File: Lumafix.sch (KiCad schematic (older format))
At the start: 6 parts, among them U1 74LS14, U2 VICII, U3 VICII_Socket

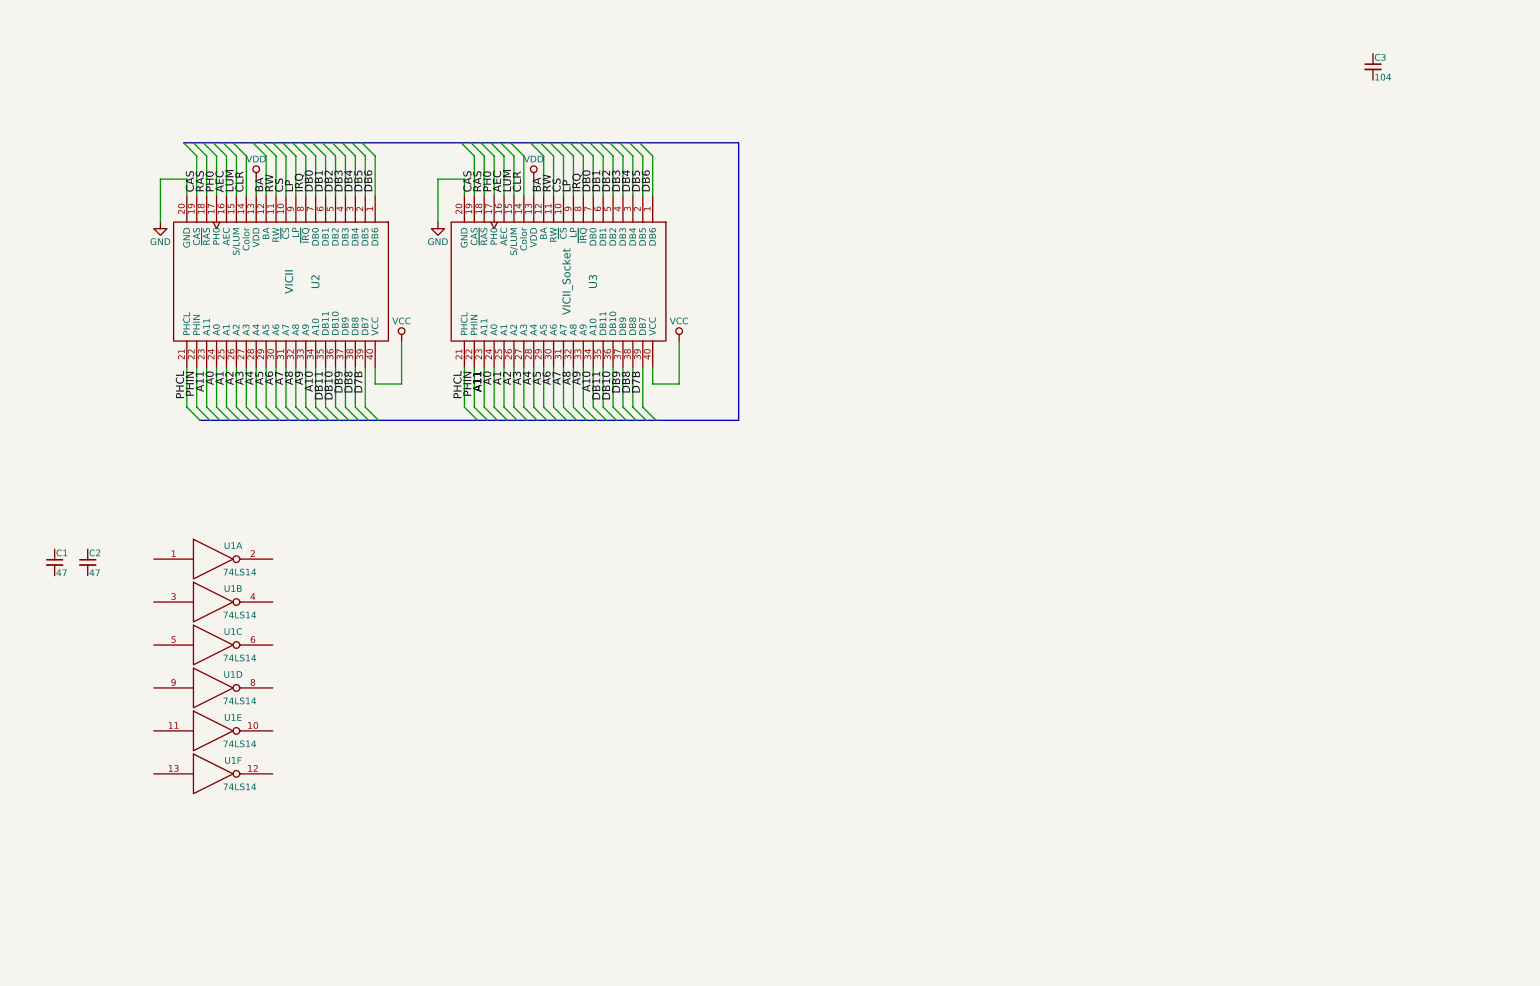
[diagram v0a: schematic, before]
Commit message: Schematic completed
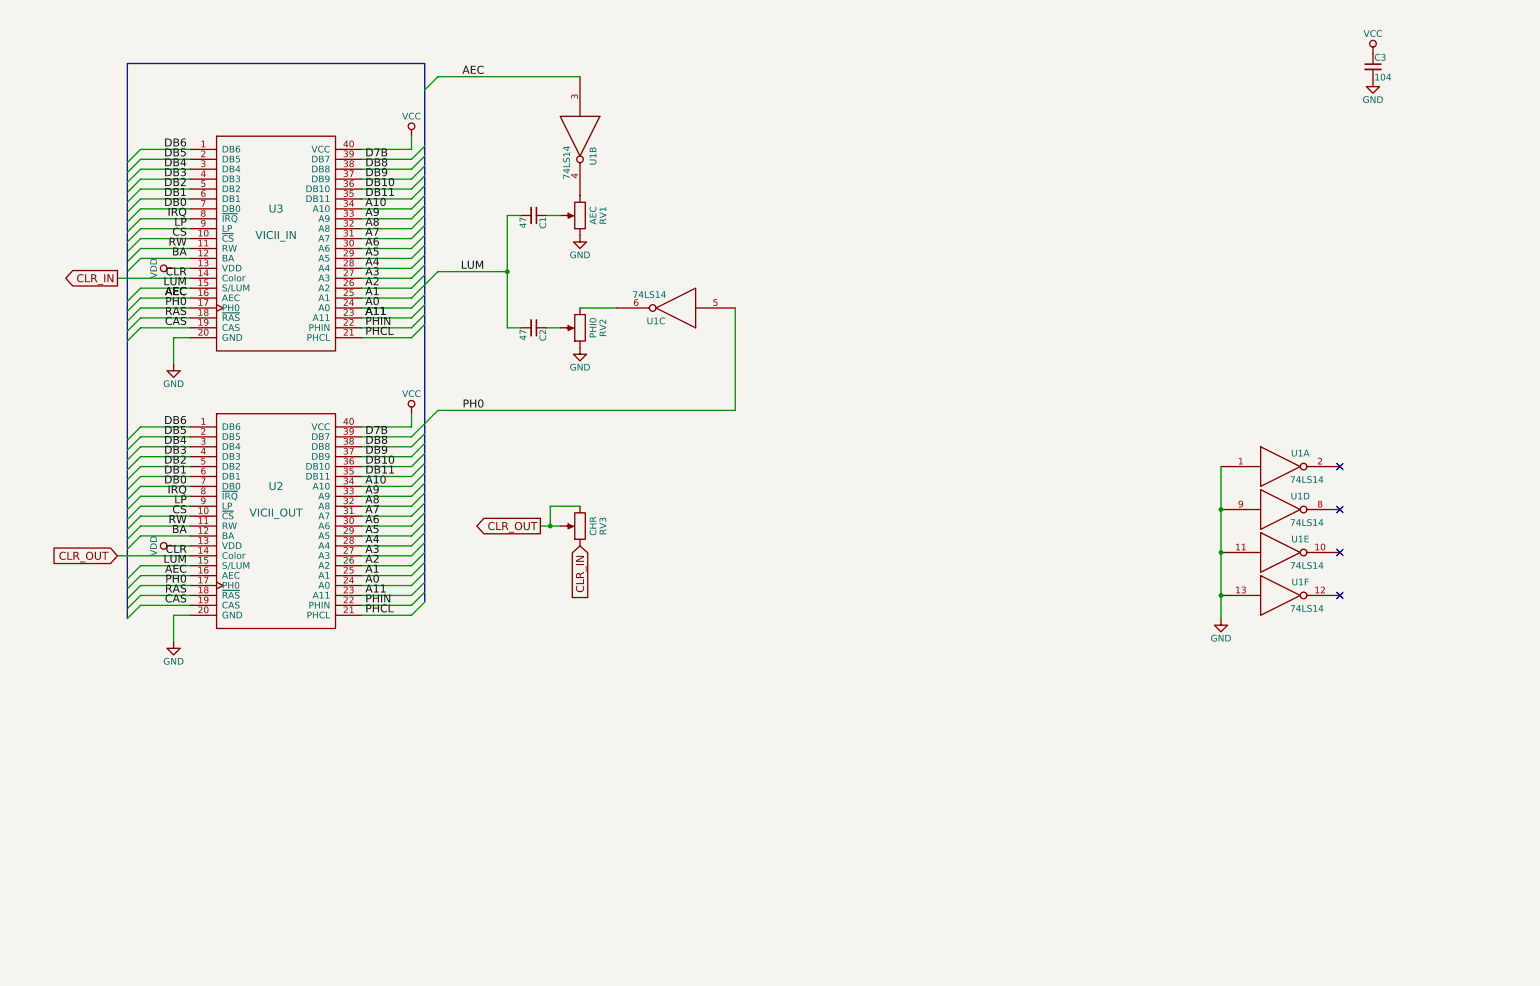
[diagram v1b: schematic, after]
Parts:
- added RV1: AEC, symbol POT
- added RV2: PHI0, symbol POT
- added RV3: CHR, symbol POT
- U2: value VICII -> VICII_OUT
- U3: value VICII_Socket -> VICII_IN
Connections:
- net AEC: now also U1.3
- net GND: now also C3.2, U1.1, U1.11, U1.13, U1.9, RV1.1, RV2.1
- net LUM: now also C1.2, C2.2
- net PH0: now also U1.5
- net VCC: now also C3.1
- net at U1.4: now also RV1.3
- net at U1.6: now also RV2.3
- net at C1.1: now also RV1.2
- net at C2.1: now also RV2.2
- net CLR renamed CLR_IN
- net CLR_IN: now also RV3.1, RV3.2, RV3.3
- no-connect marks 0 -> 4
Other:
- moved on the sheet: C1, C2, U1A, U1B, U1C, U1D, U1E, U1F, U2, U3

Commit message: PCB layout and gerber export
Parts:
- C1, C2, C3: footprint (none) -> Capacitors_THT:C_Disc_D4.7mm_W2.5mm_P5.00mm
- RV1, RV2, RV3: footprint (none) -> Potentiometers:Potentiometer_Trimmer_Bourns_3296W
- U1: footprint (none) -> Housings_DIP:DIP-14_W7.62mm_Socket
- U2: footprint (none) -> Housings_DIP:DIP-40_W15.24mm
- U3: footprint (none) -> Housings_DIP:DIP-40_W15.24mm_Socket
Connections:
- net CLR_IN: no longer RV3.2, RV3.3, U2.14 (Color)
- new net CLR_OUT: RV3.2, RV3.3, U2.14 (Color)
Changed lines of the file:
@@
 F 0 "U2" H 2525 4500 60  0000 C CNN
 F 1 "VICII_OUT" H 2525 4300 60  0000 C CNN
-F 2 "" H 2525 4300 60  0001 C CNN
+F 2 "Housings_DIP:DIP-40_W15.24mm" H 2525 4300 60  0001 C CNN
 F 3 "" H 2525 4300 60  0001 C CNN
 	1    2525 4300
@@
 F 0 "U1" H 10275 4050 50  0000 C CNN
 F 1 "74LS14" H 10325 3850 50  0000 C CNN
-F 2 "" H 10125 3950 50  0001 C CNN
+F 2 "Housings_DIP:DIP-14_W7.62mm_Socket" H 10125 3950 50  0001 C CNN
 F 3 "" H 10125 3950 50  0001 C CNN
 	1    10125 3950
@@
 F 0 "U1" H 4975 1550 50  0000 C CNN
 F 1 "74LS14" H 5025 1350 50  0000 C CNN
-F 2 "" H 4825 1450 50  0001 C CNN
+F 2 "Housings_DIP:DIP-14_W7.62mm_Socket" H 4825 1450 50  0001 C CNN
 F 3 "" H 4825 1450 50  0001 C CNN
 	2    4825 1450
@@
 F 0 "U1" H 5700 2850 50  0000 C CNN
 F 1 "74LS14" H 5750 2650 50  0000 C CNN
-F 2 "" H 5550 2750 50  0001 C CNN
+F 2 "Housings_DIP:DIP-14_W7.62mm_Socket" H 5550 2750 50  0001 C CNN
 F 3 "" H 5550 2750 50  0001 C CNN
 	3    5550 2750
@@
 F 0 "U1" H 10275 4375 50  0000 C CNN
 F 1 "74LS14" H 10325 4175 50  0000 C CNN
-F 2 "" H 10125 4275 50  0001 C CNN
+F 2 "Housings_DIP:DIP-14_W7.62mm_Socket" H 10125 4275 50  0001 C CNN
 F 3 "" H 10125 4275 50  0001 C CNN
 	4    10125 4275
@@
 F 0 "U1" H 10275 4700 50  0000 C CNN
 F 1 "74LS14" H 10325 4500 50  0000 C CNN
-F 2 "" H 10125 4600 50  0001 C CNN
+F 2 "Housings_DIP:DIP-14_W7.62mm_Socket" H 10125 4600 50  0001 C CNN
 F 3 "" H 10125 4600 50  0001 C CNN
 	5    10125 4600
@@
 F 0 "U1" H 10275 5025 50  0000 C CNN
 F 1 "74LS14" H 10325 4825 50  0000 C CNN
-F 2 "" H 10125 4925 50  0001 C CNN
+F 2 "Housings_DIP:DIP-14_W7.62mm_Socket" H 10125 4925 50  0001 C CNN
 F 3 "" H 10125 4925 50  0001 C CNN
 	6    10125 4925
@@
 F 0 "C1" H 4485 2120 50  0000 L CNN
 F 1 "47" H 4485 1970 50  0000 L CNN
-F 2 "" H 4475 2050 50  0001 C CNN
+F 2 "Capacitors_THT:C_Disc_D4.7mm_W2.5mm_P5.00mm" H 4475 2050 50  0001 C CNN
 F 3 "" H 4475 2050 50  0001 C CNN
 	1    4475 2050
@@
 F 0 "C2" H 4485 2970 50  0000 L CNN
 F 1 "47" H 4485 2820 50  0000 L CNN
-F 2 "" H 4475 2900 50  0001 C CNN
+F 2 "Capacitors_THT:C_Disc_D4.7mm_W2.5mm_P5.00mm" H 4475 2900 50  0001 C CNN
 F 3 "" H 4475 2900 50  0001 C CNN
 	1    4475 2900
@@
 F 0 "C3" H 10835 995 50  0000 L CNN
 F 1 "104" H 10835 845 50  0000 L CNN
-F 2 "" H 10825 925 50  0001 C CNN
+F 2 "Capacitors_THT:C_Disc_D4.7mm_W2.5mm_P5.00mm" H 10825 925 50  0001 C CNN
 F 3 "" H 10825 925 50  0001 C CNN
 	1    10825 925
@@
 Text Label 1850 4700 2    60   ~ 0
 LUM
-Text Label 1850 4625 2    60   ~ 0
-CLR
 Text Label 1850 4475 2    60   ~ 0
 BA
@@
 F 0 "U3" H 2525 2400 60  0000 C CNN
 F 1 "VICII_IN" H 2525 2200 60  0000 C CNN
-F 2 "" H 2525 2200 60  0001 C CNN
+F 2 "Housings_DIP:DIP-40_W15.24mm_Socket" H 2525 2200 60  0001 C CNN
 F 3 "" H 2525 2200 60  0001 C CNN
 	1    2525 2200
@@
 Text Label 1850 2600 2    60   ~ 0
 LUM
-Text Label 1850 2525 2    60   ~ 0
-CLR
 Text Label 1850 2375 2    60   ~ 0
 BA
@@
 F 0 "RV1" V 4650 2050 50  0000 C CNN
 F 1 "AEC" V 4725 2050 50  0000 C CNN
-F 2 "" H 4825 2050 50  0001 C CNN
+F 2 "Potentiometers:Potentiometer_Trimmer_Bourns_3296W" H 4825 2050 50  0001 C CNN
 F 3 "" H 4825 2050 50  0001 C CNN
 	1    4825 2050
@@
 F 0 "RV2" V 4650 2900 50  0000 C CNN
 F 1 "PHI0" V 4725 2900 50  0000 C CNN
-F 2 "" H 4825 2900 50  0001 C CNN
+F 2 "Potentiometers:Potentiometer_Trimmer_Bourns_3296W" H 4825 2900 50  0001 C CNN
 F 3 "" H 4825 2900 50  0001 C CNN
 	1    4825 2900
@@
 F 0 "RV3" V 4650 4400 50  0000 C CNN
 F 1 "CHR" V 4725 4400 50  0000 C CNN
-F 2 "" H 4825 4400 50  0001 C CNN
+F 2 "Potentiometers:Potentiometer_Trimmer_Bourns_3296W" H 4825 4400 50  0001 C CNN
 F 3 "" H 4825 4400 50  0001 C CNN
 	1    4825 4400
@@
 	3550 1550 3550 1450
 $Comp
-L GND #PWR?
+L GND #PWR07
 U 1 1 5B99D4D6
 P 4825 2200
-F 0 "#PWR?" H 4825 1950 50  0001 C CNN
+F 0 "#PWR07" H 4825 1950 50  0001 C CNN
 F 1 "GND" H 4825 2050 50  0000 C CNN
 F 2 "" H 4825 2200 50  0001 C CNN
@@
 $EndComp
 $Comp
-L GND #PWR?
+L GND #PWR08
 U 1 1 5B99D50B
 P 4825 3050
-F 0 "#PWR?" H 4825 2800 50  0001 C CNN
+F 0 "#PWR08" H 4825 2800 50  0001 C CNN
 F 1 "GND" H 4825 2900 50  0000 C CNN
 F 2 "" H 4825 3050 50  0001 C CNN
@@
 	6000 3525 6000 2750
 $Comp
-L GND #PWR?
+L GND #PWR09
 U 1 1 5B9A3666
 P 9675 5100
-F 0 "#PWR?" H 9675 4850 50  0001 C CNN
+F 0 "#PWR09" H 9675 4850 50  0001 C CNN
 F 1 "GND" H 9675 4950 50  0000 C CNN
 F 2 "" H 9675 5100 50  0001 C CNN
@@
 NoConn ~ 10575 4925
 $Comp
-L GND #PWR?
+L GND #PWR010
 U 1 1 5B9A40AD
 P 10825 1025
-F 0 "#PWR?" H 10825 775 50  0001 C CNN
+F 0 "#PWR010" H 10825 775 50  0001 C CNN
 F 1 "GND" H 10825 875 50  0000 C CNN
 F 2 "" H 10825 1025 50  0001 C CNN
@@
 $EndComp
 $Comp
-L VCC #PWR?
+L VCC #PWR011
 U 1 1 5B9A42CC
 P 10825 825
-F 0 "#PWR?" H 10825 675 50  0001 C CNN
+F 0 "#PWR011" H 10825 675 50  0001 C CNN
 F 1 "VCC" H 10825 975 50  0000 C CNN
 F 2 "" H 10825 825 50  0001 C CNN

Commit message: Exported schematic
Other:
- note added: "C64 Lumafix"
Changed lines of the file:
@@
 	1    0    0    -1
 $EndComp
+Text Notes 7375 7500 0    60   ~ 0
+C64 Lumafix
 $EndSCHEMATC

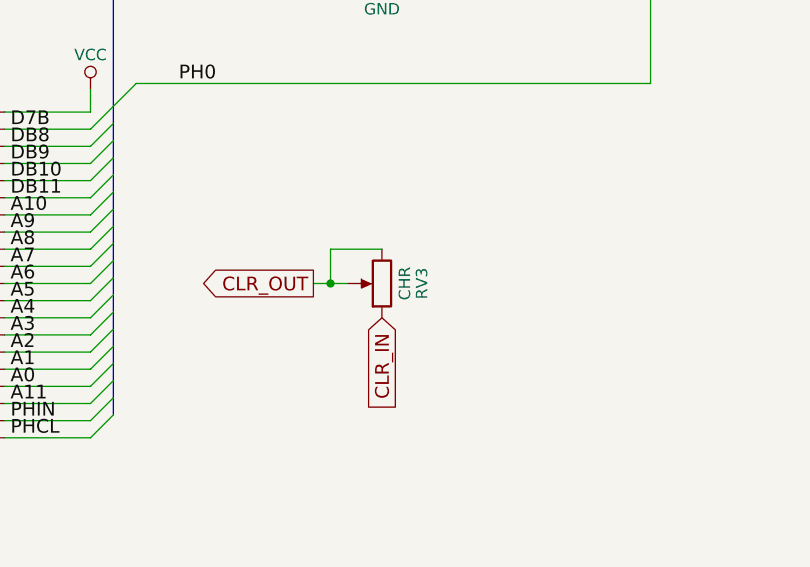
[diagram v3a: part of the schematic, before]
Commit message: Misspelled CLR on PCB, oops!
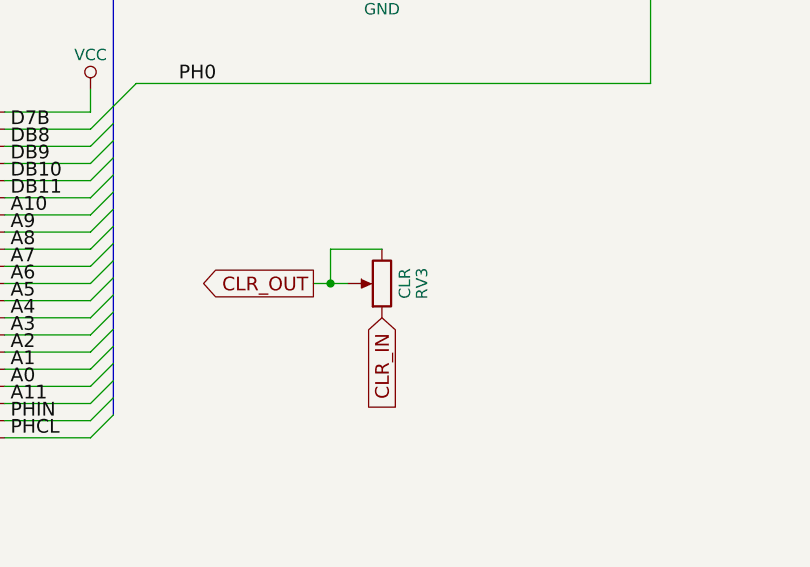
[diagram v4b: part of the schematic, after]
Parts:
- RV3: value CHR -> CLR
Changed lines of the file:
@@
 P 4825 4400
 F 0 "RV3" V 4650 4400 50  0000 C CNN
-F 1 "CHR" V 4725 4400 50  0000 C CNN
+F 1 "CLR" V 4725 4400 50  0000 C CNN
 F 2 "Potentiometers:Potentiometer_Trimmer_Bourns_3296W" H 4825 4400 50  0001 C CNN
 F 3 "" H 4825 4400 50  0001 C CNN

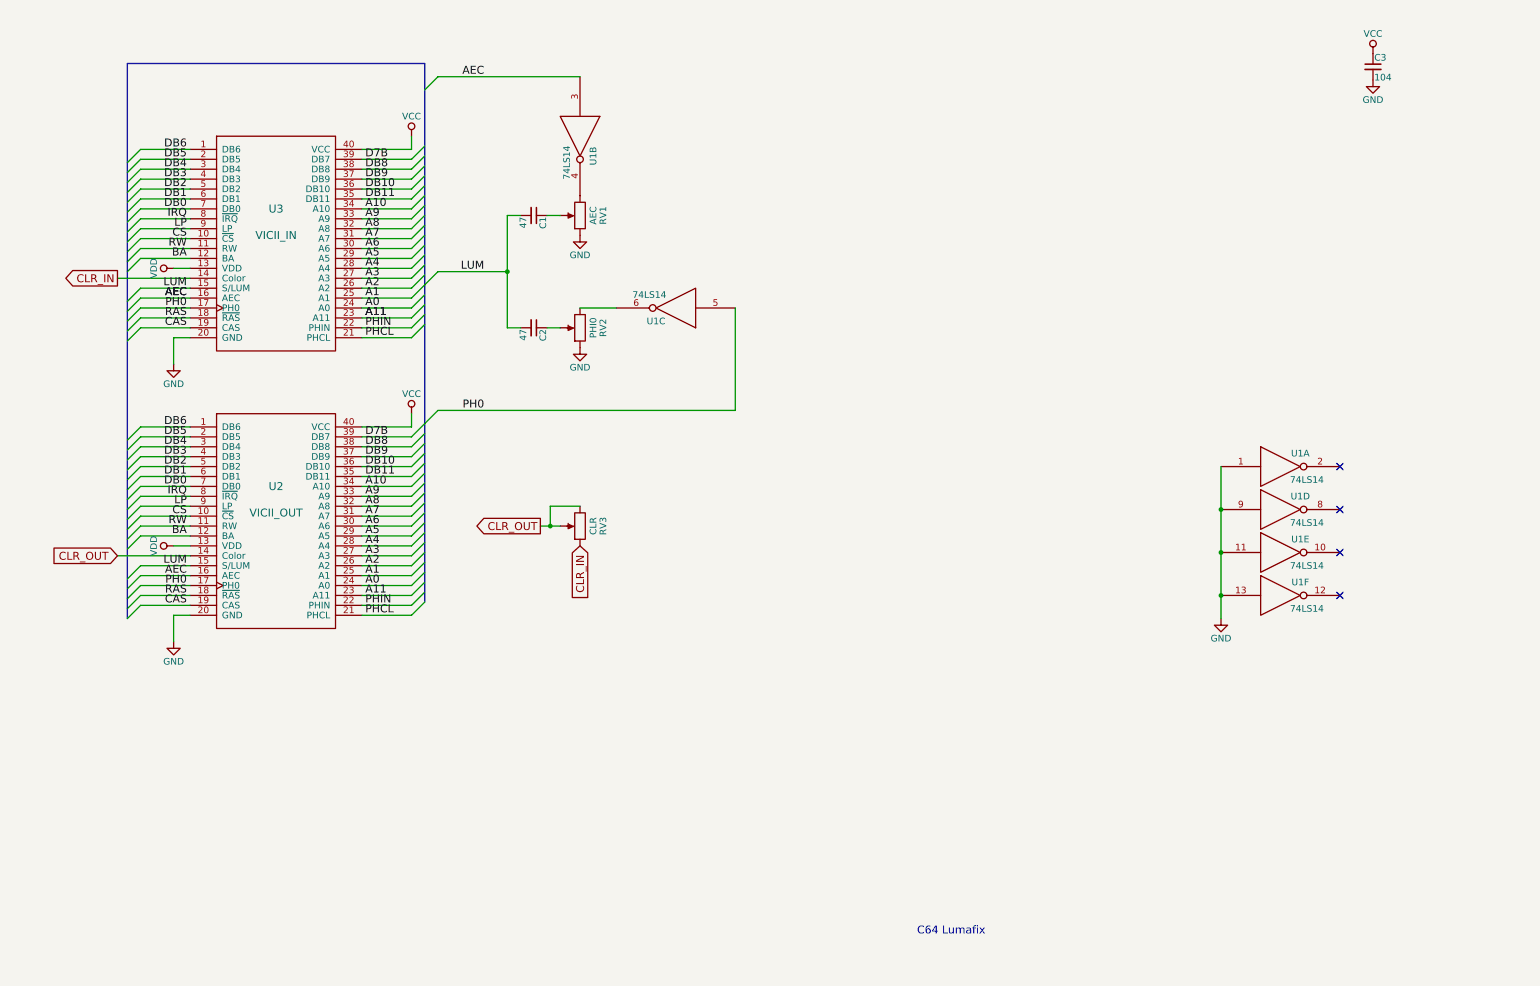
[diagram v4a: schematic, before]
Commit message: Added signal bypass to module as rev. B
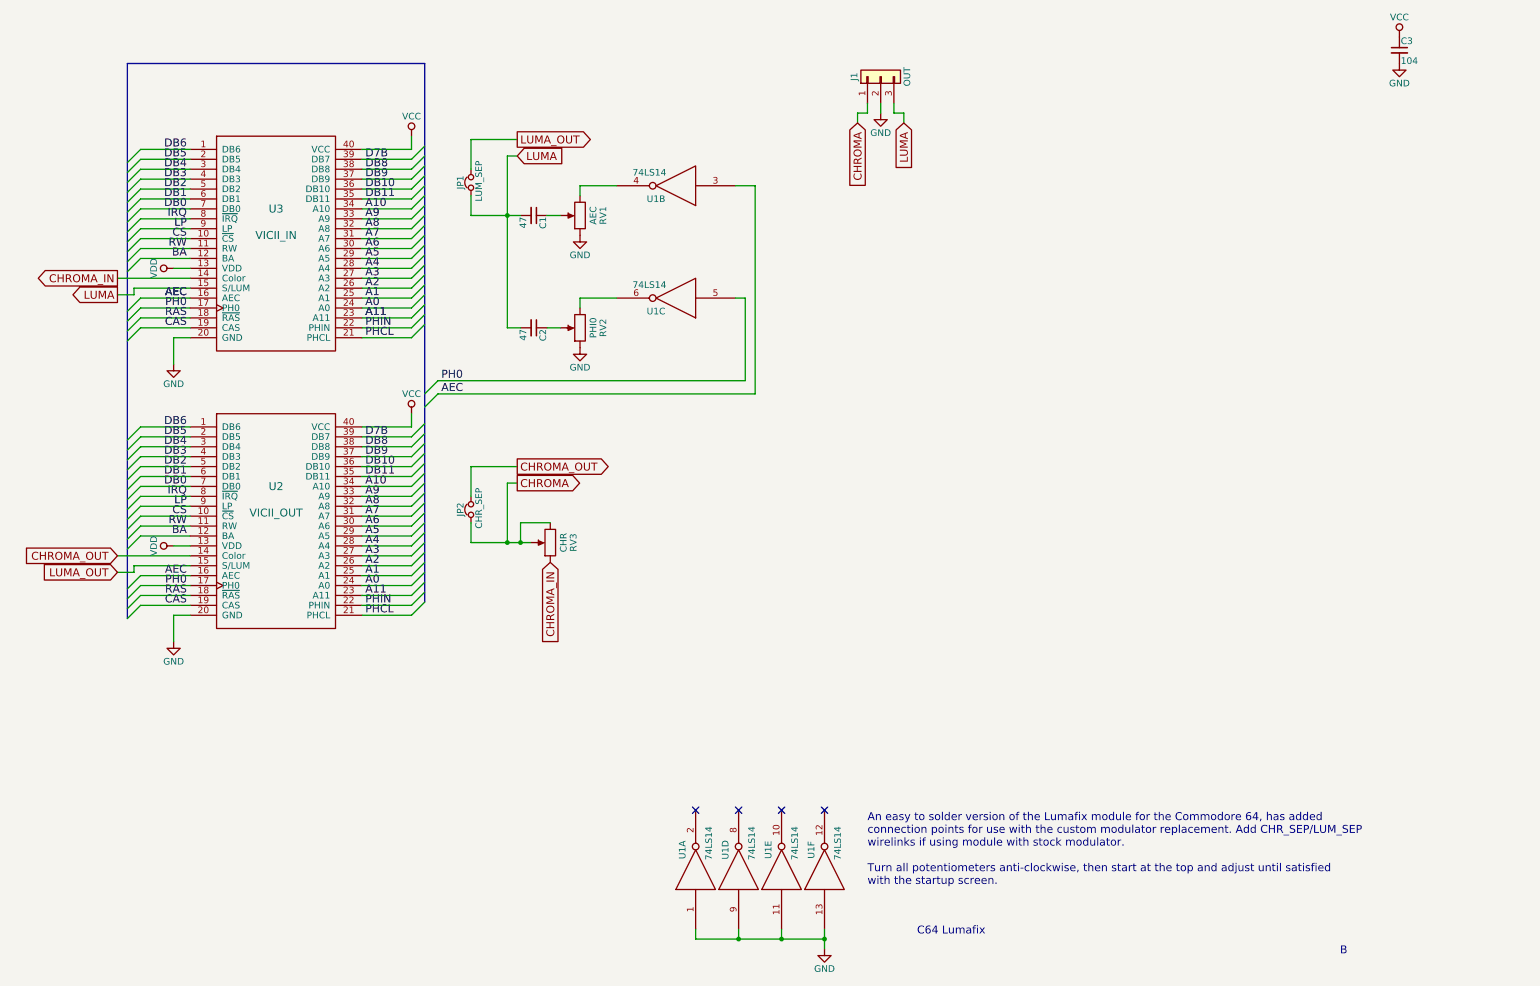
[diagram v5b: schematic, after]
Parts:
- added J1: OUT, Pin_Headers:Pin_Header_Straight_1x03_Pitch2.54mm, symbol Conn_01x03
- added JP1: LUM_SEP, Pin_Headers:Pin_Header_Straight_1x02_Pitch2.54mm, symbol Jumper_NC_Small
- added JP2: CHR_SEP, Pin_Headers:Pin_Header_Straight_1x02_Pitch2.54mm, symbol Jumper_NC_Small
- RV3: value CLR -> CHR
- U2: footprint Housings_DIP:DIP-40_W15.24mm -> VICII_OUT:VICII_OUT
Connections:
- net GND: now also J1.2 (Pin_2)
- net CLR_IN renamed CHROMA_IN
- net CLR_OUT renamed CHROMA
- net CHROMA: now also J1.1 (Pin_1), JP2.1; no longer U2.14 (Color)
- net LUM renamed LUMA
- net LUMA: now also J1.3 (Pin_3), JP1.1; no longer U2.15 (S/LUM)
- new net CHROMA_OUT: JP2.2, U2.14 (Color)
- new net LUMA_OUT: JP1.2, U2.15 (S/LUM)
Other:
- note added: "An easy to solder version of the Lumafix module for the Commodore 64, has added\nconnection points for use with the custom modulator replacement. Add CHR_SEP/LUM_SEP\nwirelinks if using module with stock modulator.\n\nTurn all potentiometers anti-clockwise, then start at the top and adjust until satisfied\nwith the startup screen."
- note added: "B"
- moved on the sheet: C3, RV3, U1A, U1B, U1C, U1D, U1E, U1F
